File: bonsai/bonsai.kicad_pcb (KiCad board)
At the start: 2 copper layers, 90.5 x 62.1 mm, 25 parts

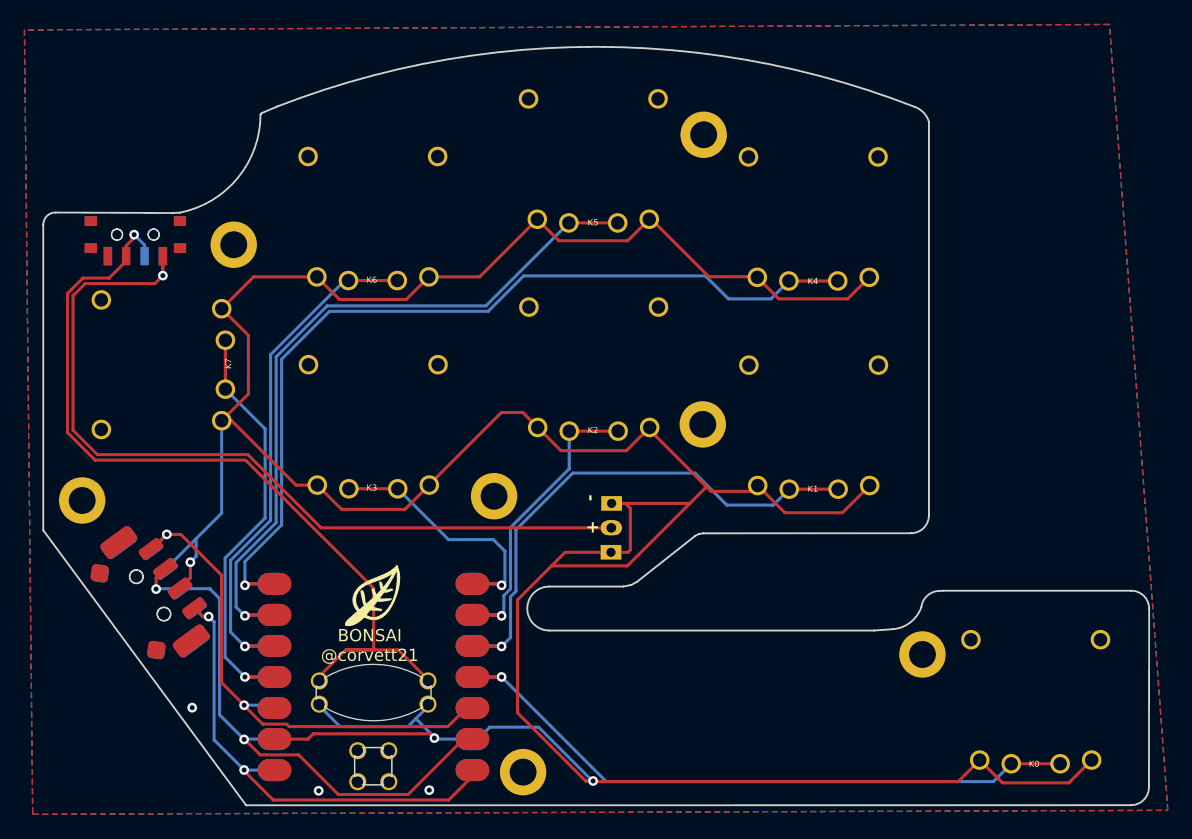
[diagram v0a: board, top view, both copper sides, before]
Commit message: Add files via upload
Made the cutout bigger for BLE interference (or lack thereof)
Moved traces away from the MCU above the ring finger key
Curved traces to look awesome
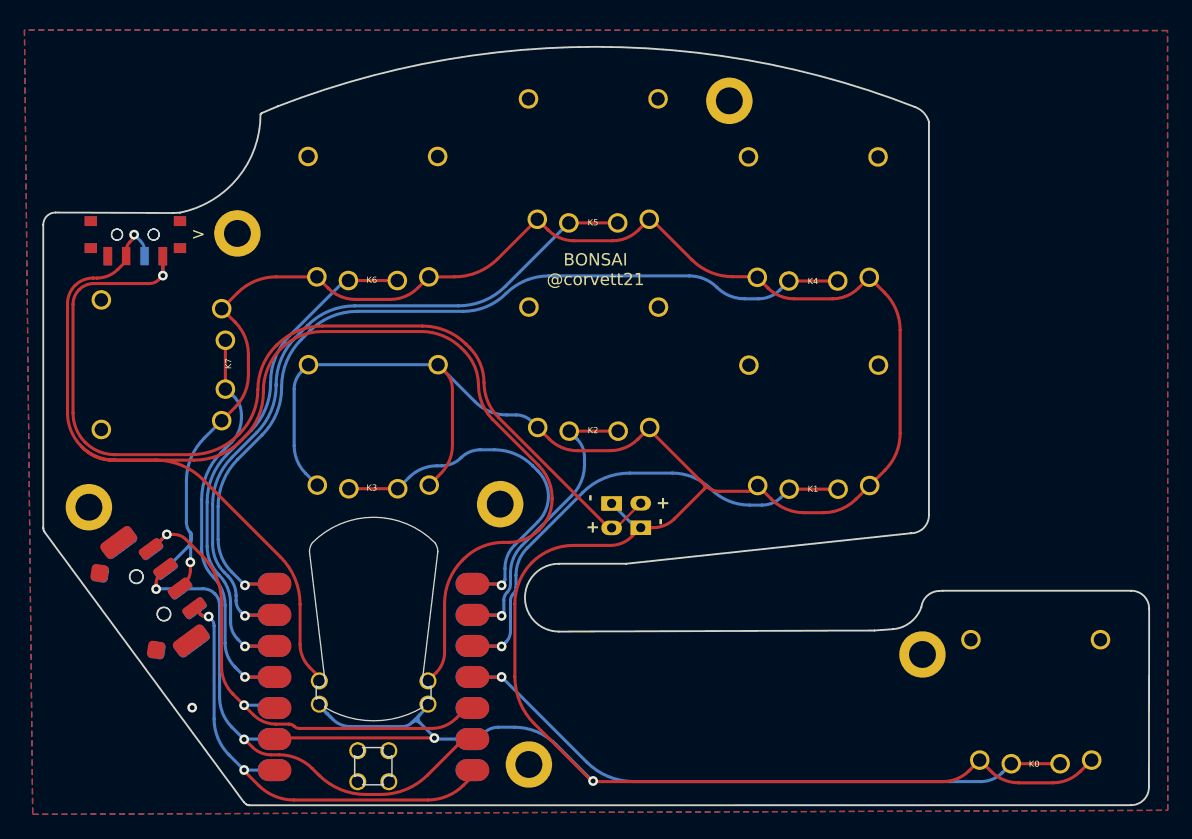
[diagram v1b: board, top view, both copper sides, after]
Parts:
- removed G*** (x2): LOGO, LOGO
- removed the REF** at (67.5, 44.5)
- moved REF** 3.48 mm to (69.7, 18.1)
- moved REF** 3.16 mm to (62.5, 53.0)
- moved REF** 0.97 mm to (29.4, 28.9)
- moved ? 0.82 mm to (51.0, 51.0)
- moved REF** 0.79 mm to (53.3, 72.3)
- moved REF** 0.78 mm to (17.3, 51.3)
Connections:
- REF** pad 4: (no net) -> GND
- REF** pad 5: (no net) -> GND
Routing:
- net RAW: track 70.4 -> 126.4 mm
- net Bat+: track 69.5 -> 83.7 mm
- net GND: track 300.6 -> 311.2 mm, vias 6 -> 4
- net K3: track 21.7 -> 31.7 mm
- net K1: track 43.8 -> 41.3 mm
- net F2: track 44.8 -> 43.6 mm
- net K7: track 34.8 -> 33.9 mm
- net F3: track 43.5 -> 42.7 mm
- net F1: track 39.9 -> 39.2 mm
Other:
- outline, holes or cut-outs redrawn
- board text added: "<"
- board text added: ">"
